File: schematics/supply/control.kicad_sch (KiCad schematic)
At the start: 66 parts, among them J10 Conn_01x04_Pin, J11 Conn_01x04_Pin, J12 Conn_01x04_Pin, J13 USBASP, J14 USBASP, J15 Conn_01x06_Pin, J16 Conn_01x06_Pin, J9 Conn_01x04_Pin, M1 Fan, Q10 IRLML5203, Q6 IRLML0030, Q9 IRLML0030, SW1 EC11W****, SW3 SW_Push, U17 ATmega328-A, U18 ATtiny1616-M, U19 Display_2.2inch_ili9341, U20 LM158DR, X1 HC-49U, 16MHz, X2 CSX-750FCC, 16MHz

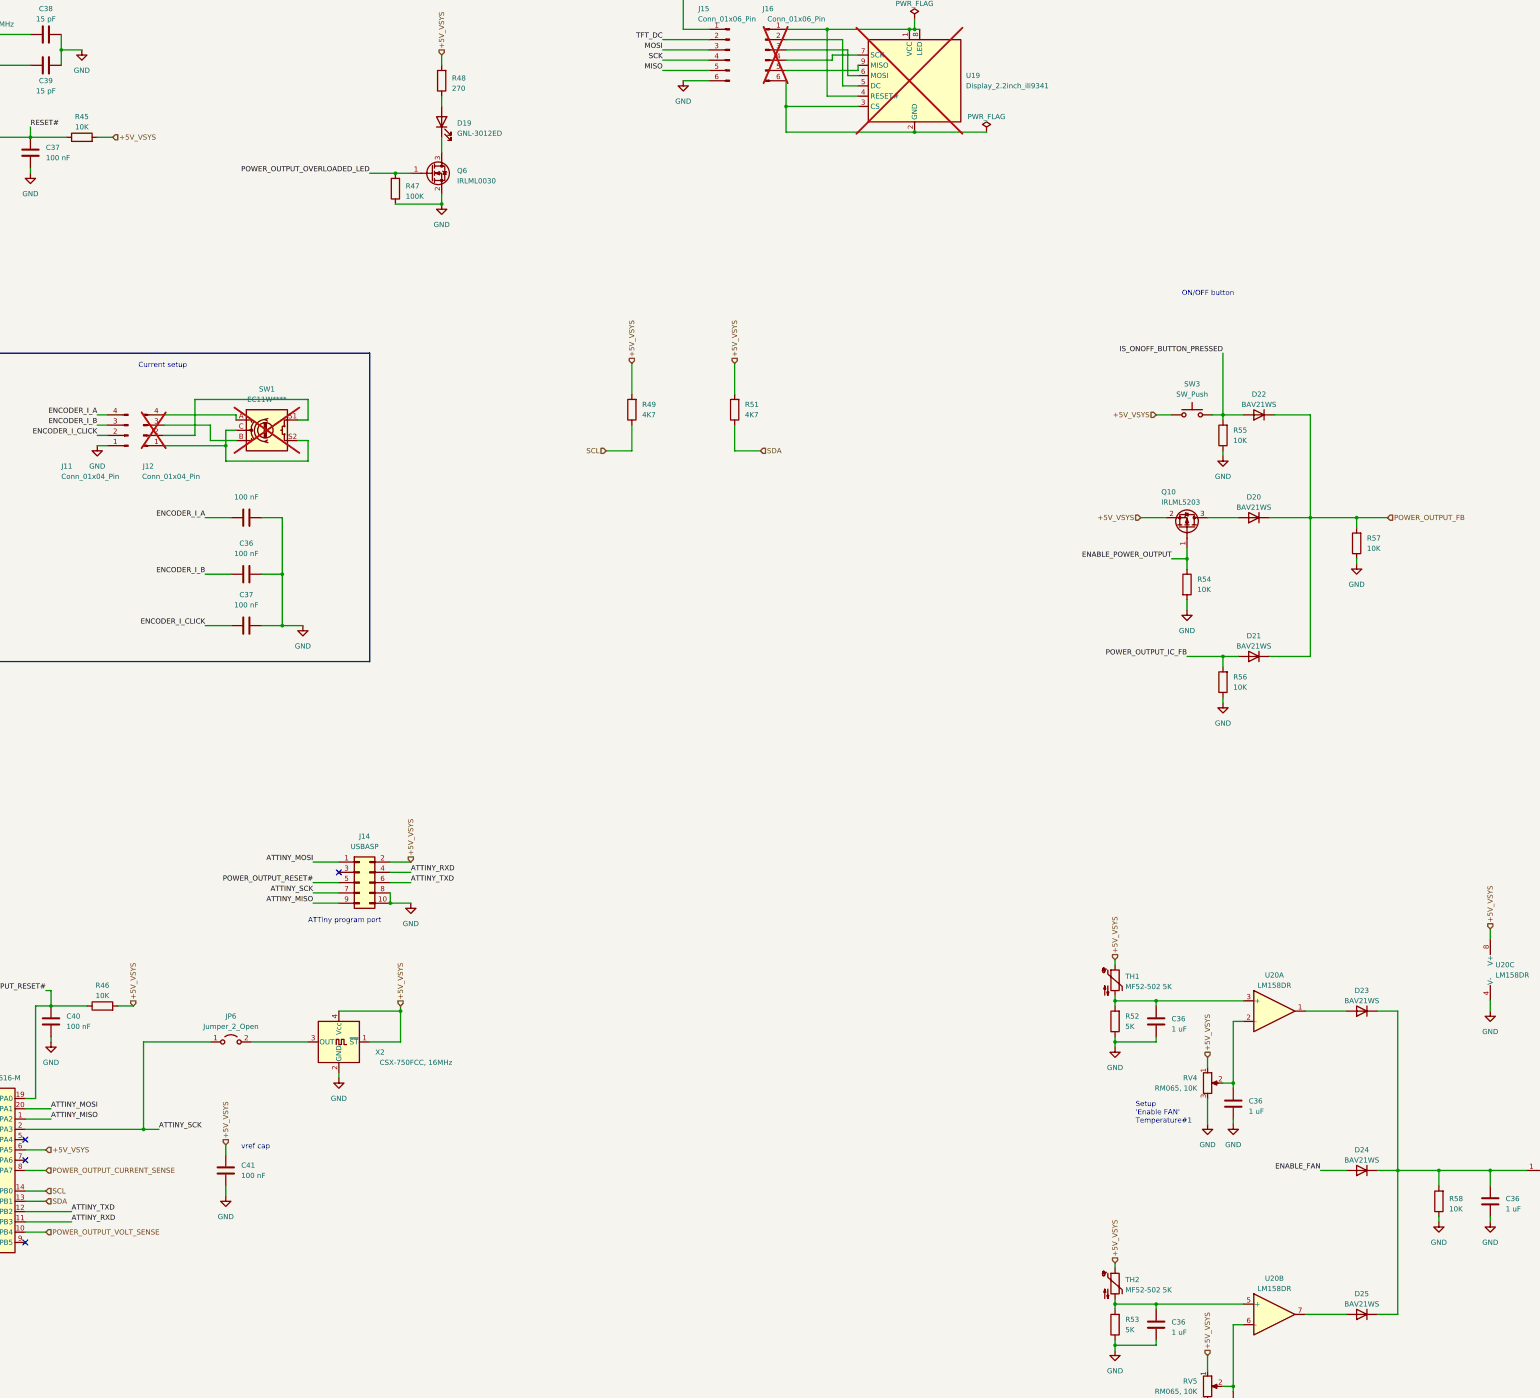
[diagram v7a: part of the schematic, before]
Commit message: One board settings changed from 4-layers to 2-layers to reduce it's price
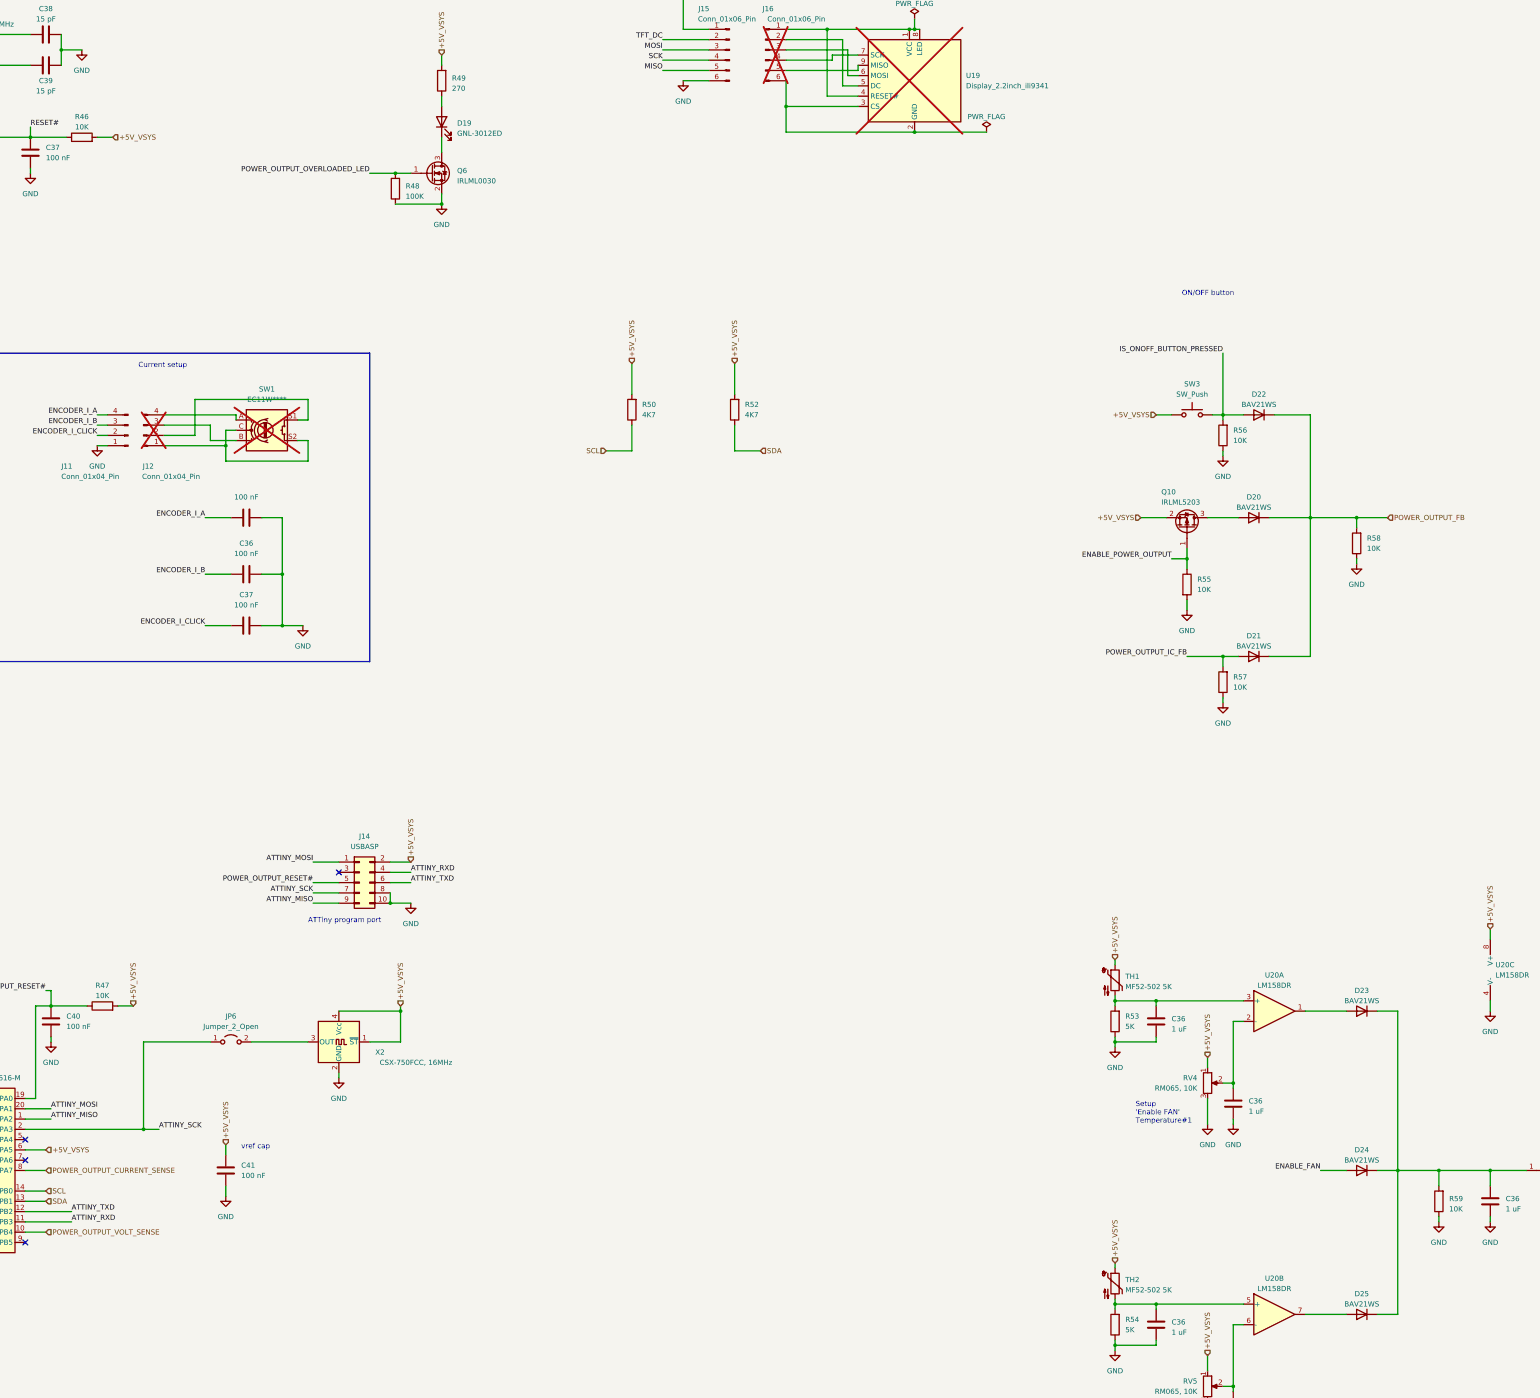
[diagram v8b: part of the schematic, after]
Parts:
- renumbered R45 to R46, R46 to R47, R47 to R48, R48 to R49, R49 to R50, R51 to R52, R52 to R53, R53 to R54, R54 to R55, R55 to R56, R56 to R57, R57 to R58, R58 to R59
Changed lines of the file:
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@@
   (symbol (lib_id "Device:R") (at 412.75 210.82 180) (unit 1)
     (in_bom yes) (on_board yes) (dnp no) (fields_autoplaced)
-    (property "Reference" "R56" (at 415.29 209.55 0)
+    (property "Reference" "R57" (at 415.29 209.55 0)
       (effects (font (size 1.27 1.27)) (justify right))
     )
@@
       (project "supply"
         (path "/1e139717-fcd1-4008-a6ea-4c993845e928/ce2ff71a-422a-4b17-921a-2433d38ec044"
-          (reference "R56") (unit 1)
+          (reference "R57") (unit 1)
         )
       )
@@
   (symbol (lib_id "Device:R") (at 135.89 290.83 90) (unit 1)
     (in_bom yes) (on_board yes) (dnp no) (fields_autoplaced)
-    (property "Reference" "R46" (at 135.89 285.75 90)
+    (property "Reference" "R47" (at 135.89 285.75 90)
       (effects (font (size 1.27 1.27)))
     )
@@
       (project "supply"
         (path "/1e139717-fcd1-4008-a6ea-4c993845e928/ce2ff71a-422a-4b17-921a-2433d38ec044"
-          (reference "R46") (unit 1)
+          (reference "R47") (unit 1)
         )
       )
@@
   (symbol (lib_id "Device:R") (at 412.75 149.86 180) (unit 1)
     (in_bom yes) (on_board yes) (dnp no) (fields_autoplaced)
-    (property "Reference" "R55" (at 415.29 148.59 0)
+    (property "Reference" "R56" (at 415.29 148.59 0)
       (effects (font (size 1.27 1.27)) (justify right))
     )
@@
       (project "supply"
         (path "/1e139717-fcd1-4008-a6ea-4c993845e928/ce2ff71a-422a-4b17-921a-2433d38ec044"
-          (reference "R55") (unit 1)
+          (reference "R56") (unit 1)
         )
       )
@@
   (symbol (lib_id "Device:R") (at 208.28 88.9 180) (unit 1)
     (in_bom yes) (on_board yes) (dnp no) (fields_autoplaced)
-    (property "Reference" "R47" (at 210.82 88.265 0)
+    (property "Reference" "R48" (at 210.82 88.265 0)
       (effects (font (size 1.27 1.27)) (justify right))
     )
@@
       (project "supply"
         (path "/1e139717-fcd1-4008-a6ea-4c993845e928/ce2ff71a-422a-4b17-921a-2433d38ec044"
-          (reference "R47") (unit 1)
+          (reference "R48") (unit 1)
         )
       )
@@
   (symbol (lib_id "Device:R") (at 219.71 62.23 180) (unit 1)
     (in_bom yes) (on_board yes) (dnp no) (fields_autoplaced)
-    (property "Reference" "R48" (at 222.25 61.595 0)
+    (property "Reference" "R49" (at 222.25 61.595 0)
       (effects (font (size 1.27 1.27)) (justify right))
     )
@@
       (project "supply"
         (path "/1e139717-fcd1-4008-a6ea-4c993845e928/ce2ff71a-422a-4b17-921a-2433d38ec044"
-          (reference "R48") (unit 1)
+          (reference "R49") (unit 1)
         )
       )
@@
   (symbol (lib_id "Device:R") (at 266.7 143.51 180) (unit 1)
     (in_bom yes) (on_board yes) (dnp no) (fields_autoplaced)
-    (property "Reference" "R49" (at 269.24 142.24 0)
+    (property "Reference" "R50" (at 269.24 142.24 0)
       (effects (font (size 1.27 1.27)) (justify right))
     )
@@
       (project "supply"
         (path "/1e139717-fcd1-4008-a6ea-4c993845e928/ce2ff71a-422a-4b17-921a-2433d38ec044"
-          (reference "R49") (unit 1)
+          (reference "R50") (unit 1)
         )
       )
@@
   (symbol (lib_id "Device:R") (at 386.08 369.57 180) (unit 1)
     (in_bom yes) (on_board yes) (dnp no) (fields_autoplaced)
-    (property "Reference" "R53" (at 388.62 368.3 0)
+    (property "Reference" "R54" (at 388.62 368.3 0)
       (effects (font (size 1.27 1.27)) (justify right))
     )
@@
       (project "supply"
         (path "/1e139717-fcd1-4008-a6ea-4c993845e928/ce2ff71a-422a-4b17-921a-2433d38ec044"
-          (reference "R53") (unit 1)
+          (reference "R54") (unit 1)
         )
       )
@@
   (symbol (lib_id "Device:R") (at 445.77 176.53 180) (unit 1)
     (in_bom yes) (on_board yes) (dnp no) (fields_autoplaced)
-    (property "Reference" "R57" (at 448.31 175.26 0)
+    (property "Reference" "R58" (at 448.31 175.26 0)
       (effects (font (size 1.27 1.27)) (justify right))
     )
@@
       (project "supply"
         (path "/1e139717-fcd1-4008-a6ea-4c993845e928/ce2ff71a-422a-4b17-921a-2433d38ec044"
-          (reference "R57") (unit 1)
+          (reference "R58") (unit 1)
         )
       )
@@
   (symbol (lib_id "Device:R") (at 130.81 76.2 90) (unit 1)
     (in_bom yes) (on_board yes) (dnp no) (fields_autoplaced)
-    (property "Reference" "R45" (at 130.81 71.12 90)
+    (property "Reference" "R46" (at 130.81 71.12 90)
       (effects (font (size 1.27 1.27)))
     )
@@
       (project "supply"
         (path "/1e139717-fcd1-4008-a6ea-4c993845e928/ce2ff71a-422a-4b17-921a-2433d38ec044"
-          (reference "R45") (unit 1)
+          (reference "R46") (unit 1)
         )
       )
@@
   (symbol (lib_id "Device:R") (at 403.86 186.69 0) (unit 1)
     (in_bom yes) (on_board yes) (dnp no) (fields_autoplaced)
-    (property "Reference" "R54" (at 406.4 185.42 0)
+    (property "Reference" "R55" (at 406.4 185.42 0)
       (effects (font (size 1.27 1.27)) (justify left))
     )
@@
       (project "supply"
         (path "/1e139717-fcd1-4008-a6ea-4c993845e928/ce2ff71a-422a-4b17-921a-2433d38ec044"
-          (reference "R54") (unit 1)
+          (reference "R55") (unit 1)
         )
       )
@@
   (symbol (lib_id "Device:R") (at 466.09 339.09 180) (unit 1)
     (in_bom yes) (on_board yes) (dnp no) (fields_autoplaced)
-    (property "Reference" "R58" (at 468.63 338.455 0)
+    (property "Reference" "R59" (at 468.63 338.455 0)
       (effects (font (size 1.27 1.27)) (justify right))
     )
@@
       (project "supply"
         (path "/1e139717-fcd1-4008-a6ea-4c993845e928/ce2ff71a-422a-4b17-921a-2433d38ec044"
-          (reference "R58") (unit 1)
+          (reference "R59") (unit 1)
         )
       )
@@
       (project "supply"
         (path "/1e139717-fcd1-4008-a6ea-4c993845e928/ce2ff71a-422a-4b17-921a-2433d38ec044"
-          (reference "R50") (unit 1)
+          (reference "R51") (unit 1)
         )
       )
@@
   (symbol (lib_id "Device:R") (at 292.1 143.51 180) (unit 1)
     (in_bom yes) (on_board yes) (dnp no) (fields_autoplaced)
-    (property "Reference" "R51" (at 294.64 142.24 0)
+    (property "Reference" "R52" (at 294.64 142.24 0)
       (effects (font (size 1.27 1.27)) (justify right))
     )
@@
       (project "supply"
         (path "/1e139717-fcd1-4008-a6ea-4c993845e928/ce2ff71a-422a-4b17-921a-2433d38ec044"
-          (reference "R51") (unit 1)
+          (reference "R52") (unit 1)
         )
       )
@@
   (symbol (lib_id "Device:R") (at 386.08 294.64 180) (unit 1)
     (in_bom yes) (on_board yes) (dnp no) (fields_autoplaced)
-    (property "Reference" "R52" (at 388.62 293.37 0)
+    (property "Reference" "R53" (at 388.62 293.37 0)
       (effects (font (size 1.27 1.27)) (justify right))
     )
@@
       (project "supply"
         (path "/1e139717-fcd1-4008-a6ea-4c993845e928/ce2ff71a-422a-4b17-921a-2433d38ec044"
-          (reference "R52") (unit 1)
-        )
-      )
+          (reference "R53") (unit 1)
+        )
+      )
